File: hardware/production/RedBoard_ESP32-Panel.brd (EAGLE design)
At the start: 242.1 x 248.9 mm, 2454 parts, among them J1 5.5x2.1mm Barrel, J101 USB C, J102 USB_SOLDER_PADS, J103 M10NO_SILK, J108 QWIIC_RIGHT_ANGLE, J109 MICRO-SDPUSH-PUSH, J110 5.5x2.1mm Barrel, J117 USB C, J118 USB_SOLDER_PADS, J119 M10NO_SILK, J124 QWIIC_RIGHT_ANGLE, J125 MICRO-SDPUSH-PUSH, J126 5.5x2.1mm Barrel, J13 QWIIC_RIGHT_ANGLE, J133 USB C, J134 USB_SOLDER_PADS, J135 M10NO_SILK, J140 QWIIC_RIGHT_ANGLE, J141 MICRO-SDPUSH-PUSH, J142 5.5x2.1mm Barrel, J149 USB C, J15 MICRO-SDPUSH-PUSH, J150 USB_SOLDER_PADS, J151 M10NO_SILK, J156 QWIIC_RIGHT_ANGLE, J157 MICRO-SDPUSH-PUSH, J158 5.5x2.1mm Barrel, J165 USB C, J166 USB_SOLDER_PADS, J167 M10NO_SILK, J172 QWIIC_RIGHT_ANGLE, J173 MICRO-SDPUSH-PUSH, J174 5.5x2.1mm Barrel, J181 USB C, J182 USB_SOLDER_PADS, J183 M10NO_SILK, J188 QWIIC_RIGHT_ANGLE, J189 MICRO-SDPUSH-PUSH, J190 5.5x2.1mm Barrel, J2 USB C, J21 USB C, J22 USB_SOLDER_PADS, J23 M10NO_SILK, J28 QWIIC_RIGHT_ANGLE, J29 MICRO-SDPUSH-PUSH, J3 USB_SOLDER_PADS, J30 5.5x2.1mm Barrel, J37 USB C, J38 USB_SOLDER_PADS, J39 M10NO_SILK, J44 QWIIC_RIGHT_ANGLE, J45 MICRO-SDPUSH-PUSH, J46 5.5x2.1mm Barrel, J5 M10NO_SILK, J53 USB C, J54 USB_SOLDER_PADS, J55 M10NO_SILK, J60 QWIIC_RIGHT_ANGLE, J61 MICRO-SDPUSH-PUSH, J62 5.5x2.1mm Barrel, J69 USB C, J70 USB_SOLDER_PADS, J71 M10NO_SILK, J76 QWIIC_RIGHT_ANGLE, J77 MICRO-SDPUSH-PUSH, J78 5.5x2.1mm Barrel, J85 USB C, J86 USB_SOLDER_PADS, J87 M10NO_SILK, J92 QWIIC_RIGHT_ANGLE, J93 MICRO-SDPUSH-PUSH, J94 5.5x2.1mm Barrel, Q1 MBT3904DW1T1, Q100 20V/4.2A/52mΩ/1.4W, Q102 20V/4.2A/52mΩ/1.4W, Q104 20V/4.2A/52mΩ/1.4W, Q105 MBT3904DW1T1, Q107 20V/4.2A/52mΩ/1.4W, Q109 20V/4.2A/52mΩ/1.4W, Q11 20V/4.2A/52mΩ/1.4W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

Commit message: Changed board per Nathan's recommendations; added production files.
- Changed SPI pins nomenclatures.
- Fixed silkscreens.
- Replaced SD card socket with an updated one.
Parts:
- J109, J125, J141, J15, J157, J173, J189, J29, J45, J61, J77, J93: value MICRO-SDPUSH-PUSH -> MICRO-SD-PUSH-PUSH-EXT-PIN; device SparkFun-Connectors:MICRO-SD-SOCKET -> SparkFun-Connectors:MICROSD-EXTERNALPIN
- J111, J112, J127, J128, J14, J143, J144, J159, J16, J160, J175, J176, J191, J192, J31, J32, J47, J48, J63, J64, J79, J80, J95, J96: device SparkFun-Connectors:1X02 -> SparkFun-Connectors:1X02_NO_SILK
- U$1000, U$1094, U$154, U$248, U$342, U$436, U$530, U$62, U$624, U$718, U$812, U$906: device output-ESP32:#IOREF#32321868 -> output-ESP32:#IOREF#321865
- U$101, U$1041, U$195, U$289, U$383, U$477, U$571, U$665, U$759, U$8, U$853, U$947: device output-ESP32:#CIPO#30 -> output-ESP32:#POCI#30
- U$1010, U$1104, U$164, U$258, U$352, U$446, U$540, U$634, U$728, U$73, U$822, U$916: device output-ESP32:#23#COPI#32321869 -> output-ESP32:#23#PICO#321866
- U$1011, U$1105, U$165, U$259, U$353, U$447, U$541, U$635, U$729, U$74, U$823, U$917: device output-ESP32:#19#CIPO#32321869 -> output-ESP32:#19#POCI#321866
- U$1016, U$1110, U$170, U$264, U$358, U$452, U$546, U$640, U$734, U$79, U$828, U$922: device output-ESP32:#GND#32321869 -> output-ESP32:#GND#321866
- U$1017, U$1111, U$171, U$265, U$359, U$453, U$547, U$641, U$735, U$80, U$829, U$923: device output-ESP32:#3#3V#32321869 -> output-ESP32:#3#3V#321866
- U$102, U$1042, U$196, U$290, U$384, U$478, U$572, U$666, U$760, U$854, U$9, U$948: device output-ESP32:#COPI#29 -> output-ESP32:#PICO#29
- U$1082, U$142, U$236, U$330, U$424, U$50, U$518, U$612, U$706, U$800, U$894, U$988: device output-ESP32:#39#A3#32321865 -> output-ESP32:#39#A3#321862
- U$1083, U$143, U$237, U$331, U$425, U$51, U$519, U$613, U$707, U$801, U$895, U$989: device output-ESP32:#36#A0#32321865 -> output-ESP32:#36#A0#321862
- U$1085, U$145, U$239, U$333, U$427, U$521, U$53, U$615, U$709, U$803, U$897, U$991: device output-ESP32:#35#A7#32321865 -> output-ESP32:#35#A7#321862
- U$1087, U$147, U$241, U$335, U$429, U$523, U$55, U$617, U$711, U$805, U$899, U$993: device output-ESP32:#33#A5#32321865 -> output-ESP32:#34#A6#321862
- U$1088, U$148, U$242, U$336, U$430, U$524, U$56, U$618, U$712, U$806, U$900, U$994: device output-ESP32:#VIN#32321865 -> output-ESP32:#VIN#321862
- U$1089, U$1092, U$149, U$152, U$243, U$246, U$337, U$340, U$431, U$434, U$525, U$528, U$57, U$60, U$619, U$622, U$713, U$716, U$807, U$810, U$901, U$904, U$995, U$998: device output-ESP32:#GND#32321866 -> output-ESP32:#GND#321863
- U$1090, U$150, U$244, U$338, U$432, U$526, U$58, U$620, U$714, U$808, U$902, U$996: device output-ESP32:#5V#32321867 -> output-ESP32:#5V#321864
- U$1091, U$151, U$245, U$339, U$433, U$527, U$59, U$621, U$715, U$809, U$903, U$997: device output-ESP32:#3#3V#32321867 -> output-ESP32:#3#3V#321864
- U$1093, U$153, U$247, U$341, U$435, U$529, U$61, U$623, U$717, U$811, U$905, U$999: device output-ESP32:##RST##32321867 -> output-ESP32:##RESET##321864
- moved R173 39.3 mm to (200.2, 64.0), turned to 270 degrees
- moved R260 39.3 mm to (200.2, 122.9), turned to 270 degrees
- moved R347 39.3 mm to (200.2, 181.9), turned to 270 degrees
- moved R86 39.3 mm to (200.2, 5.08), turned to 270 degrees
- moved LOGO1 36.8 mm to (15.4, 28.4), turned to 270 degrees
- moved LOGO16 36.8 mm to (15.4, 87.4), turned to 270 degrees
- moved LOGO31 36.8 mm to (15.4, 146.3), turned to 270 degrees
- moved LOGO46 36.8 mm to (15.4, 205.2), turned to 270 degrees
- moved R144 36.3 mm to (124.2, 64.0), turned to 270 degrees
- moved R231 36.3 mm to (124.2, 122.9), turned to 270 degrees
- moved R318 36.3 mm to (124.2, 181.9), turned to 270 degrees
- moved R57 36.3 mm to (124.2, 5.08), turned to 270 degrees
- moved LOGO21 34.1 mm to (91.3, 87.4), turned to 270 degrees
- moved LOGO5 34.1 mm to (91.3, 28.4), turned to 270 degrees
- moved LOGO36 34.1 mm to (91.3, 146.3), turned to 270 degrees
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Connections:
- removed net ESP32_GPIO19_CIPO: J15.DO/DAT0, J5.6, J6.6A, J6.6B, U1.31
- removed net ESP32_GPIO19_CIPO1: J17.6A, J17.6B, J23.6, J29.DO/DAT0, U8.31
- removed net ESP32_GPIO19_CIPO10: J161.6A, J161.6B, J167.6, J173.DO/DAT0, U62.31
- removed net ESP32_GPIO19_CIPO11: J177.6A, J177.6B, J183.6, J189.DO/DAT0, U68.31
- removed net ESP32_GPIO19_CIPO2: J33.6A, J33.6B, J39.6, J45.DO/DAT0, U14.31
- removed net ESP32_GPIO19_CIPO3: J49.6A, J49.6B, J55.6, J61.DO/DAT0, U20.31
- removed net ESP32_GPIO19_CIPO4: J65.6A, J65.6B, J71.6, J77.DO/DAT0, U26.31
- removed net ESP32_GPIO19_CIPO5: J81.6A, J81.6B, J87.6, J93.DO/DAT0, U32.31
- removed net ESP32_GPIO19_CIPO6: J103.6, J109.DO/DAT0, J97.6A, J97.6B, U38.31
- removed net ESP32_GPIO19_CIPO7: J113.6A, J113.6B, J119.6, J125.DO/DAT0, U44.31
- removed net ESP32_GPIO19_CIPO8: J129.6A, J129.6B, J135.6, J141.DO/DAT0, U50.31
- removed net ESP32_GPIO19_CIPO9: J145.6A, J145.6B, J151.6, J157.DO/DAT0, U56.31
- removed net ESP32_GPIO23_COPI: J15.DI/CMD, J5.7, J6.7A, J6.7B, U1.37
- removed net ESP32_GPIO23_COPI1: J17.7A, J17.7B, J23.7, J29.DI/CMD, U8.37
- removed net ESP32_GPIO23_COPI10: J161.7A, J161.7B, J167.7, J173.DI/CMD, U62.37
- removed net ESP32_GPIO23_COPI11: J177.7A, J177.7B, J183.7, J189.DI/CMD, U68.37
- removed net ESP32_GPIO23_COPI2: J33.7A, J33.7B, J39.7, J45.DI/CMD, U14.37
- removed net ESP32_GPIO23_COPI3: J49.7A, J49.7B, J55.7, J61.DI/CMD, U20.37
- removed net ESP32_GPIO23_COPI4: J65.7A, J65.7B, J71.7, J77.DI/CMD, U26.37
- removed net ESP32_GPIO23_COPI5: J81.7A, J81.7B, J87.7, J93.DI/CMD, U32.37
- removed net ESP32_GPIO23_COPI6: J103.7, J109.DI/CMD, J97.7A, J97.7B, U38.37
- removed net ESP32_GPIO23_COPI7: J113.7A, J113.7B, J119.7, J125.DI/CMD, U44.37
- removed net ESP32_GPIO23_COPI8: J129.7A, J129.7B, J135.7, J141.DI/CMD, U50.37
- removed net ESP32_GPIO23_COPI9: J145.7A, J145.7B, J151.7, J157.DI/CMD, U56.37
- removed net GND1: C18.2, C19.2, C20.-, C21.2, C22.2, C23.2, C24.2, C25.2, C26.-, C27.2, C28.-, C29.2, C30.2, C31.2, C32.2, C33.2, C34.2, J17.4A, J17.4B, J18.6, J18.7, J21.GND, J21.GND2, J22.GND, J23.4, J24.6, J24.7, J27.3, J27.5, J27.7, J27.9, J28.1, J29.GND, J29.GND1, J29.GND3, J30.GND, J32.2, JP27.1, Q17.1, Q17.4, R32.1, R33.1, R37.1, R40.1, R42.1, R43.1, R47.1, R48.1, R49.1, R50.1, R52.1, R53.1, R54.1, R55.1, R56.1, R58.1, S3.1, S3.2, S4.1, S4.2, U10.2, U11.2, U12.1, U12.4, U12.6, U12.9, U7.1, U8.1, U8.15, U8.38, U8.GND1, U8.GNDT1, U8.GNDT2, U8.GNDT3, U8.GNDT4, U8.GNDT5, U8.GNDT6, U8.GNDT7, U8.GNDT8
- removed net GND11: C188.2, C189.2, C190.-, C191.2, C192.2, C193.2, C194.2, C195.2, C196.-, C197.2, C198.-, C199.2, C200.2, C201.2, C202.2, C203.2, C204.2, J177.4A, J177.4B, J178.6, J178.7, J181.GND, J181.GND2, J182.GND, J183.4, J184.6, J184.7, J187.3, J187.5, J187.7, J187.9, J188.1, J189.GND, J189.GND1, J189.GND3, J190.GND, J192.2, JP167.1, Q147.1, Q147.4, R322.1, R323.1, R327.1, R330.1, R332.1, R333.1, R337.1, R338.1, R339.1, R340.1, R342.1, R343.1, R344.1, R345.1, R346.1, R348.1, S23.1, S23.2, S24.1, S24.2, U67.1, U68.1, U68.15, U68.38, U68.GND1, U68.GNDT1, U68.GNDT2, U68.GNDT3, U68.GNDT4, U68.GNDT5, U68.GNDT6, U68.GNDT7, U68.GNDT8, U70.2, U71.2, U72.1, U72.4, U72.6, U72.9
- removed net GND3: C52.2, C53.2, C54.-, C55.2, C56.2, C57.2, C58.2, C59.2, C60.-, C61.2, C62.-, C63.2, C64.2, C65.2, C66.2, C67.2, C68.2, J49.4A, J49.4B, J50.6, J50.7, J53.GND, J53.GND2, J54.GND, J55.4, J56.6, J56.7, J59.3, J59.5, J59.7, J59.9, J60.1, J61.GND, J61.GND1, J61.GND3, J62.GND, J64.2, JP55.1, Q43.1, Q43.4, R100.1, R101.1, R105.1, R106.1, R107.1, R108.1, R110.1, R111.1, R112.1, R113.1, R114.1, R116.1, R90.1, R91.1, R95.1, R98.1, S7.1, S7.2, S8.1, S8.2, U19.1, U20.1, U20.15, U20.38, U20.GND1, U20.GNDT1, U20.GNDT2, U20.GNDT3, U20.GNDT4, U20.GNDT5, U20.GNDT6, U20.GNDT7, U20.GNDT8, U22.2, U23.2, U24.1, U24.4, U24.6, U24.9
- removed net GND5: C100.2, C101.2, C102.2, C86.2, C87.2, C88.-, C89.2, C90.2, C91.2, C92.2, C93.2, C94.-, C95.2, C96.-, C97.2, C98.2, C99.2, J81.4A, J81.4B, J82.6, J82.7, J85.GND, J85.GND2, J86.GND, J87.4, J88.6, J88.7, J91.3, J91.5, J91.7, J91.9, J92.1, J93.GND, J93.GND1, J93.GND3, J94.GND, J96.2, JP83.1, Q69.1, Q69.4, R148.1, R149.1, R153.1, R156.1, R158.1, R159.1, R163.1, R164.1, R165.1, R166.1, R168.1, R169.1, R170.1, R171.1, R172.1, R174.1, S11.1, S11.2, S12.1, S12.2, U31.1, U32.1, U32.15, U32.38, U32.GND1, U32.GNDT1, U32.GNDT2, U32.GNDT3, U32.GNDT4, U32.GNDT5, U32.GNDT6, U32.GNDT7, U32.GNDT8, U34.2, U35.2, U36.1, U36.4, U36.6, U36.9
- removed net GND7: C120.2, C121.2, C122.-, C123.2, C124.2, C125.2, C126.2, C127.2, C128.-, C129.2, C130.-, C131.2, C132.2, C133.2, C134.2, C135.2, C136.2, J113.4A, J113.4B, J114.6, J114.7, J117.GND, J117.GND2, J118.GND, J119.4, J120.6, J120.7, J123.3, J123.5, J123.7, J123.9, J124.1, J125.GND, J125.GND1, J125.GND3, J126.GND, J128.2, JP111.1, Q95.1, Q95.4, R206.1, R207.1, R211.1, R214.1, R216.1, R217.1, R221.1, R222.1, R223.1, R224.1, R226.1, R227.1, R228.1, R229.1, R230.1, R232.1, S15.1, S15.2, S16.1, S16.2, U43.1, U44.1, U44.15, U44.38, U44.GND1, U44.GNDT1, U44.GNDT2, U44.GNDT3, U44.GNDT4, U44.GNDT5, U44.GNDT6, U44.GNDT7, U44.GNDT8, U46.2, U47.2, U48.1, U48.4, U48.6, U48.9
- removed net GND9: C154.2, C155.2, C156.-, C157.2, C158.2, C159.2, C160.2, C161.2, C162.-, C163.2, C164.-, C165.2, C166.2, C167.2, C168.2, C169.2, C170.2, J145.4A, J145.4B, J146.6, J146.7, J149.GND, J149.GND2, J150.GND, J151.4, J152.6, J152.7, J155.3, J155.5, J155.7, J155.9, J156.1, J157.GND, J157.GND1, J157.GND3, J158.GND, J160.2, JP139.1, Q121.1, Q121.4, R264.1, R265.1, R269.1, R272.1, R274.1, R275.1, R279.1, R280.1, R281.1, R282.1, R284.1, R285.1, R286.1, R287.1, R288.1, R290.1, S19.1, S19.2, S20.1, S20.2, U55.1, U56.1, U56.15, U56.38, U56.GND1, U56.GNDT1, U56.GNDT2, U56.GNDT3, U56.GNDT4, U56.GNDT5, U56.GNDT6, U56.GNDT7, U56.GNDT8, U58.2, U59.2, U60.1, U60.4, U60.6, U60.9
- new net ESP32_GPIO19_POCI: J15.7, J5.6, J6.6A, J6.6B, U1.31
- new net ESP32_GPIO19_POCI1: J17.6A, J17.6B, J23.6, J29.7, U8.31
- new net ESP32_GPIO19_POCI10: J161.6A, J161.6B, J167.6, J173.7, U62.31
- new net ESP32_GPIO19_POCI11: J177.6A, J177.6B, J183.6, J189.7, U68.31
- new net ESP32_GPIO19_POCI2: J33.6A, J33.6B, J39.6, J45.7, U14.31
- new net ESP32_GPIO19_POCI3: J49.6A, J49.6B, J55.6, J61.7, U20.31
- new net ESP32_GPIO19_POCI4: J65.6A, J65.6B, J71.6, J77.7, U26.31
- new net ESP32_GPIO19_POCI5: J81.6A, J81.6B, J87.6, J93.7, U32.31
- new net ESP32_GPIO19_POCI6: J103.6, J109.7, J97.6A, J97.6B, U38.31
- new net ESP32_GPIO19_POCI7: J113.6A, J113.6B, J119.6, J125.7, U44.31
- new net ESP32_GPIO19_POCI8: J129.6A, J129.6B, J135.6, J141.7, U50.31
- new net ESP32_GPIO19_POCI9: J145.6A, J145.6B, J151.6, J157.7, U56.31
- new net ESP32_GPIO23_PICO: J15.3, J5.7, J6.7A, J6.7B, U1.37
- new net ESP32_GPIO23_PICO1: J17.7A, J17.7B, J23.7, J29.3, U8.37
- new net ESP32_GPIO23_PICO10: J161.7A, J161.7B, J167.7, J173.3, U62.37
- new net ESP32_GPIO23_PICO11: J177.7A, J177.7B, J183.7, J189.3, U68.37
- new net ESP32_GPIO23_PICO2: J33.7A, J33.7B, J39.7, J45.3, U14.37
- new net ESP32_GPIO23_PICO3: J49.7A, J49.7B, J55.7, J61.3, U20.37
- new net ESP32_GPIO23_PICO4: J65.7A, J65.7B, J71.7, J77.3, U26.37
- new net ESP32_GPIO23_PICO5: J81.7A, J81.7B, J87.7, J93.3, U32.37
- new net ESP32_GPIO23_PICO6: J103.7, J109.3, J97.7A, J97.7B, U38.37
- new net ESP32_GPIO23_PICO7: J113.7A, J113.7B, J119.7, J125.3, U44.37
- new net ESP32_GPIO23_PICO8: J129.7A, J129.7B, J135.7, J141.3, U50.37
- new net ESP32_GPIO23_PICO9: J145.7A, J145.7B, J151.7, J157.3, U56.37
- new net GND12: C103.2, C104.2, C105.-, C106.2, C107.2, C108.2, C109.2, C110.2, C111.-, C112.2, C113.-, C114.2, C115.2, C116.2, C117.2, C118.2, C119.2, J101.GND, J101.GND2, J102.GND, J103.4, J104.6, J104.7, J107.3, J107.5, J107.7, J107.9, J108.1, J109.10, J109.11, J109.12, J109.13, J109.6, J110.GND, J112.2, J97.4A, J97.4B, J98.6, J98.7, JP97.1, Q82.1, Q82.4, R177.1, R178.1, R182.1, R185.1, R187.1, R188.1, R192.1, R193.1, R194.1, R195.1, R197.1, R198.1, R199.1, R200.1, R201.1, R203.1, S13.1, S13.2, S14.1, S14.2, U37.1, U38.1, U38.15, U38.38, U38.GND1, U38.GNDT1, U38.GNDT2, U38.GNDT3, U38.GNDT4, U38.GNDT5, U38.GNDT6, U38.GNDT7, U38.GNDT8, U40.2, U41.2, U42.1, U42.4, U42.6, U42.9
- new net GND14: C120.2, C121.2, C122.-, C123.2, C124.2, C125.2, C126.2, C127.2, C128.-, C129.2, C130.-, C131.2, C132.2, C133.2, C134.2, C135.2, C136.2, J113.4A, J113.4B, J114.6, J114.7, J117.GND, J117.GND2, J118.GND, J119.4, J120.6, J120.7, J123.3, J123.5, J123.7, J123.9, J124.1, J125.10, J125.11, J125.12, J125.13, J125.6, J126.GND, J128.2, JP111.1, Q95.1, Q95.4, R206.1, R207.1, R211.1, R214.1, R216.1, R217.1, R221.1, R222.1, R223.1, R224.1, R226.1, R227.1, R228.1, R229.1, R230.1, R232.1, S15.1, S15.2, S16.1, S16.2, U43.1, U44.1, U44.15, U44.38, U44.GND1, U44.GNDT1, U44.GNDT2, U44.GNDT3, U44.GNDT4, U44.GNDT5, U44.GNDT6, U44.GNDT7, U44.GNDT8, U46.2, U47.2, U48.1, U48.4, U48.6, U48.9
- new net GND16: C137.2, C138.2, C139.-, C140.2, C141.2, C142.2, C143.2, C144.2, C145.-, C146.2, C147.-, C148.2, C149.2, C150.2, C151.2, C152.2, C153.2, J129.4A, J129.4B, J130.6, J130.7, J133.GND, J133.GND2, J134.GND, J135.4, J136.6, J136.7, J139.3, J139.5, J139.7, J139.9, J140.1, J141.10, J141.11, J141.12, J141.13, J141.6, J142.GND, J144.2, JP125.1, Q108.1, Q108.4, R235.1, R236.1, R240.1, R243.1, R245.1, R246.1, R250.1, R251.1, R252.1, R253.1, R255.1, R256.1, R257.1, R258.1, R259.1, R261.1, S17.1, S17.2, S18.1, S18.2, U49.1, U50.1, U50.15, U50.38, U50.GND1, U50.GNDT1, U50.GNDT2, U50.GNDT3, U50.GNDT4, U50.GNDT5, U50.GNDT6, U50.GNDT7, U50.GNDT8, U52.2, U53.2, U54.1, U54.4, U54.6, U54.9
- new net GND18: C154.2, C155.2, C156.-, C157.2, C158.2, C159.2, C160.2, C161.2, C162.-, C163.2, C164.-, C165.2, C166.2, C167.2, C168.2, C169.2, C170.2, J145.4A, J145.4B, J146.6, J146.7, J149.GND, J149.GND2, J150.GND, J151.4, J152.6, J152.7, J155.3, J155.5, J155.7, J155.9, J156.1, J157.10, J157.11, J157.12, J157.13, J157.6, J158.GND, J160.2, JP139.1, Q121.1, Q121.4, R264.1, R265.1, R269.1, R272.1, R274.1, R275.1, R279.1, R280.1, R281.1, R282.1, R284.1, R285.1, R286.1, R287.1, R288.1, R290.1, S19.1, S19.2, S20.1, S20.2, U55.1, U56.1, U56.15, U56.38, U56.GND1, U56.GNDT1, U56.GNDT2, U56.GNDT3, U56.GNDT4, U56.GNDT5, U56.GNDT6, U56.GNDT7, U56.GNDT8, U58.2, U59.2, U60.1, U60.4, U60.6, U60.9
- new net GND20: C171.2, C172.2, C173.-, C174.2, C175.2, C176.2, C177.2, C178.2, C179.-, C180.2, C181.-, C182.2, C183.2, C184.2, C185.2, C186.2, C187.2, J161.4A, J161.4B, J162.6, J162.7, J165.GND, J165.GND2, J166.GND, J167.4, J168.6, J168.7, J171.3, J171.5, J171.7, J171.9, J172.1, J173.10, J173.11, J173.12, J173.13, J173.6, J174.GND, J176.2, JP153.1, Q134.1, Q134.4, R293.1, R294.1, R298.1, R301.1, R303.1, R304.1, R308.1, R309.1, R310.1, R311.1, R313.1, R314.1, R315.1, R316.1, R317.1, R319.1, S21.1, S21.2, S22.1, S22.2, U61.1, U62.1, U62.15, U62.38, U62.GND1, U62.GNDT1, U62.GNDT2, U62.GNDT3, U62.GNDT4, U62.GNDT5, U62.GNDT6, U62.GNDT7, U62.GNDT8, U64.2, U65.2, U66.1, U66.4, U66.6, U66.9
- new net GND22: C188.2, C189.2, C190.-, C191.2, C192.2, C193.2, C194.2, C195.2, C196.-, C197.2, C198.-, C199.2, C200.2, C201.2, C202.2, C203.2, C204.2, J177.4A, J177.4B, J178.6, J178.7, J181.GND, J181.GND2, J182.GND, J183.4, J184.6, J184.7, J187.3, J187.5, J187.7, J187.9, J188.1, J189.10, J189.11, J189.12, J189.13, J189.6, J190.GND, J192.2, JP167.1, Q147.1, Q147.4, R322.1, R323.1, R327.1, R330.1, R332.1, R333.1, R337.1, R338.1, R339.1, R340.1, R342.1, R343.1, R344.1, R345.1, R346.1, R348.1, S23.1, S23.2, S24.1, S24.2, U67.1, U68.1, U68.15, U68.38, U68.GND1, U68.GNDT1, U68.GNDT2, U68.GNDT3, U68.GNDT4, U68.GNDT5, U68.GNDT6, U68.GNDT7, U68.GNDT8, U70.2, U71.2, U72.1, U72.4, U72.6, U72.9
- net 3.3V: now also J15.4; no longer J15.VCC
- net 3.3V1: now also J29.4; no longer J29.VCC
- net 3.3V10: now also J173.4; no longer J173.VCC
- net 3.3V11: now also J189.4; no longer J189.VCC
- net 3.3V2: now also J45.4; no longer J45.VCC
- net 3.3V3: now also J61.4; no longer J61.VCC
- net 3.3V4: now also J77.4; no longer J77.VCC
- net 3.3V5: now also J93.4; no longer J93.VCC
- net 3.3V6: now also J109.4; no longer J109.VCC
- net 3.3V7: now also J125.4; no longer J125.VCC
- net 3.3V8: now also J141.4; no longer J141.VCC
- net 3.3V9: now also J157.4; no longer J157.VCC
- net ESP32_GPIO18_SCK: now also J15.5; no longer J15.SCLK
- net ESP32_GPIO18_SCK1: now also J29.5; no longer J29.SCLK
- net ESP32_GPIO18_SCK10: now also J173.5; no longer J173.SCLK
- net ESP32_GPIO18_SCK11: now also J189.5; no longer J189.SCLK
- net ESP32_GPIO18_SCK2: now also J45.5; no longer J45.SCLK
- net ESP32_GPIO18_SCK3: now also J61.5; no longer J61.SCLK
- net ESP32_GPIO18_SCK4: now also J77.5; no longer J77.SCLK
- net ESP32_GPIO18_SCK5: now also J93.5; no longer J93.SCLK
- net ESP32_GPIO18_SCK6: now also J109.5; no longer J109.SCLK
- net ESP32_GPIO18_SCK7: now also J125.5; no longer J125.SCLK
- net ESP32_GPIO18_SCK8: now also J141.5; no longer J141.SCLK
- net ESP32_GPIO18_SCK9: now also J157.5; no longer J157.SCLK
- net ESP32_GPIO5_!CS!: now also J15.2; no longer J15.CS/DAT3
- net ESP32_GPIO5_!CS!1: now also J29.2; no longer J29.CS/DAT3
- net ESP32_GPIO5_!CS!10: now also J173.2; no longer J173.CS/DAT3
- net ESP32_GPIO5_!CS!11: now also J189.2; no longer J189.CS/DAT3
- net ESP32_GPIO5_!CS!2: now also J45.2; no longer J45.CS/DAT3
- net ESP32_GPIO5_!CS!3: now also J61.2; no longer J61.CS/DAT3
- net ESP32_GPIO5_!CS!4: now also J77.2; no longer J77.CS/DAT3
- net ESP32_GPIO5_!CS!5: now also J93.2; no longer J93.CS/DAT3
- net ESP32_GPIO5_!CS!6: now also J109.2; no longer J109.CS/DAT3
- net ESP32_GPIO5_!CS!7: now also J125.2; no longer J125.CS/DAT3
- net ESP32_GPIO5_!CS!8: now also J141.2; no longer J141.CS/DAT3
- net ESP32_GPIO5_!CS!9: now also J157.2; no longer J157.CS/DAT3
- net GND: now also J15.10, J15.11, J15.12, J15.13, J15.6; no longer J15.GND, J15.GND1, J15.GND3
- net GND10: now also C100.2, C101.2, C102.2, C86.2, C87.2, C88.-, C89.2, C90.2, C91.2, C92.2, C93.2, C94.-, C95.2, C96.-, C97.2, C98.2, C99.2, J81.4A, J81.4B, J82.6, J82.7, J85.GND, J85.GND2, J86.GND, J87.4, J88.6, J88.7, J91.3, J91.5, J91.7, J91.9, J92.1, J93.10, J93.11, J93.12, J93.13, J93.6, J94.GND, J96.2, JP83.1, Q69.1, Q69.4, R148.1, R149.1, R153.1, R156.1, R158.1, R159.1, R163.1, R164.1, R165.1, R166.1, R168.1, R169.1, R170.1, R171.1, R172.1, R174.1, S11.1, S11.2, S12.1, S12.2, U31.1, U32.1, U32.15, U32.38, U32.GND1, U32.GNDT1, U32.GNDT2, U32.GNDT3, U32.GNDT4, U32.GNDT5, U32.GNDT6, U32.GNDT7, U32.GNDT8, U34.2, U35.2, U36.1, U36.4, U36.6, U36.9; no longer C171.2, C172.2, C173.-, C174.2, C175.2, C176.2, C177.2, C178.2, C179.-, C180.2, C181.-, C182.2, C183.2, C184.2, C185.2, C186.2, C187.2, J161.4A, J161.4B, J162.6, J162.7, J165.GND, J165.GND2, J166.GND, J167.4, J168.6, J168.7, J171.3, J171.5, J171.7, J171.9, J172.1, J173.GND, J173.GND1, J173.GND3, J174.GND, J176.2, JP153.1, Q134.1, Q134.4, R293.1, R294.1, R298.1, R301.1, R303.1, R304.1, R308.1, R309.1, R310.1, R311.1, R313.1, R314.1, R315.1, R316.1, R317.1, R319.1, S21.1, S21.2, S22.1, S22.2, U61.1, U62.1, U62.15, U62.38, U62.GND1, U62.GNDT1, U62.GNDT2, U62.GNDT3, U62.GNDT4, U62.GNDT5, U62.GNDT6, U62.GNDT7, U62.GNDT8, U64.2, U65.2, U66.1, U66.4, U66.6, U66.9
- net GND2: now also C18.2, C19.2, C20.-, C21.2, C22.2, C23.2, C24.2, C25.2, C26.-, C27.2, C28.-, C29.2, C30.2, C31.2, C32.2, C33.2, C34.2, J17.4A, J17.4B, J18.6, J18.7, J21.GND, J21.GND2, J22.GND, J23.4, J24.6, J24.7, J27.3, J27.5, J27.7, J27.9, J28.1, J29.10, J29.11, J29.12, J29.13, J29.6, J30.GND, J32.2, JP27.1, Q17.1, Q17.4, R32.1, R33.1, R37.1, R40.1, R42.1, R43.1, R47.1, R48.1, R49.1, R50.1, R52.1, R53.1, R54.1, R55.1, R56.1, R58.1, S3.1, S3.2, S4.1, S4.2, U10.2, U11.2, U12.1, U12.4, U12.6, U12.9, U7.1, U8.1, U8.15, U8.38, U8.GND1, U8.GNDT1, U8.GNDT2, U8.GNDT3, U8.GNDT4, U8.GNDT5, U8.GNDT6, U8.GNDT7, U8.GNDT8; no longer C35.2, C36.2, C37.-, C38.2, C39.2, C40.2, C41.2, C42.2, C43.-, C44.2, C45.-, C46.2, C47.2, C48.2, C49.2, C50.2, C51.2, J33.4A, J33.4B, J34.6, J34.7, J37.GND, J37.GND2, J38.GND, J39.4, J40.6, J40.7, J43.3, J43.5, J43.7, J43.9, J44.1, J45.GND, J45.GND1, J45.GND3, J46.GND, J48.2, JP41.1, Q30.1, Q30.4, R61.1, R62.1, R66.1, R69.1, R71.1, R72.1, R76.1, R77.1, R78.1, R79.1, R81.1, R82.1, R83.1, R84.1, R85.1, R87.1, S5.1, S5.2, S6.1, S6.2, U13.1, U14.1, U14.15, U14.38, U14.GND1, U14.GNDT1, U14.GNDT2, U14.GNDT3, U14.GNDT4, U14.GNDT5, U14.GNDT6, U14.GNDT7, U14.GNDT8, U16.2, U17.2, U18.1, U18.4, U18.6, U18.9
- net GND4: now also C35.2, C36.2, C37.-, C38.2, C39.2, C40.2, C41.2, C42.2, C43.-, C44.2, C45.-, C46.2, C47.2, C48.2, C49.2, C50.2, C51.2, J33.4A, J33.4B, J34.6, J34.7, J37.GND, J37.GND2, J38.GND, J39.4, J40.6, J40.7, J43.3, J43.5, J43.7, J43.9, J44.1, J45.10, J45.11, J45.12, J45.13, J45.6, J46.GND, J48.2, JP41.1, Q30.1, Q30.4, R61.1, R62.1, R66.1, R69.1, R71.1, R72.1, R76.1, R77.1, R78.1, R79.1, R81.1, R82.1, R83.1, R84.1, R85.1, R87.1, S5.1, S5.2, S6.1, S6.2, U13.1, U14.1, U14.15, U14.38, U14.GND1, U14.GNDT1, U14.GNDT2, U14.GNDT3, U14.GNDT4, U14.GNDT5, U14.GNDT6, U14.GNDT7, U14.GNDT8, U16.2, U17.2, U18.1, U18.4, U18.6, U18.9; no longer C69.2, C70.2, C71.-, C72.2, C73.2, C74.2, C75.2, C76.2, C77.-, C78.2, C79.-, C80.2, C81.2, C82.2, C83.2, C84.2, C85.2, J65.4A, J65.4B, J66.6, J66.7, J69.GND, J69.GND2, J70.GND, J71.4, J72.6, J72.7, J75.3, J75.5, J75.7, J75.9, J76.1, J77.GND, J77.GND1, J77.GND3, J78.GND, J80.2, JP69.1, Q56.1, Q56.4, R119.1, R120.1, R124.1, R127.1, R129.1, R130.1, R134.1, R135.1, R136.1, R137.1, R139.1, R140.1, R141.1, R142.1, R143.1, R145.1, S10.1, S10.2, S9.1, S9.2, U25.1, U26.1, U26.15, U26.38, U26.GND1, U26.GNDT1, U26.GNDT2, U26.GNDT3, U26.GNDT4, U26.GNDT5, U26.GNDT6, U26.GNDT7, U26.GNDT8, U28.2, U29.2, U30.1, U30.4, U30.6, U30.9
- net GND6: now also C52.2, C53.2, C54.-, C55.2, C56.2, C57.2, C58.2, C59.2, C60.-, C61.2, C62.-, C63.2, C64.2, C65.2, C66.2, C67.2, C68.2, J49.4A, J49.4B, J50.6, J50.7, J53.GND, J53.GND2, J54.GND, J55.4, J56.6, J56.7, J59.3, J59.5, J59.7, J59.9, J60.1, J61.10, J61.11, J61.12, J61.13, J61.6, J62.GND, J64.2, JP55.1, Q43.1, Q43.4, R100.1, R101.1, R105.1, R106.1, R107.1, R108.1, R110.1, R111.1, R112.1, R113.1, R114.1, R116.1, R90.1, R91.1, R95.1, R98.1, S7.1, S7.2, S8.1, S8.2, U19.1, U20.1, U20.15, U20.38, U20.GND1, U20.GNDT1, U20.GNDT2, U20.GNDT3, U20.GNDT4, U20.GNDT5, U20.GNDT6, U20.GNDT7, U20.GNDT8, U22.2, U23.2, U24.1, U24.4, U24.6, U24.9; no longer C103.2, C104.2, C105.-, C106.2, C107.2, C108.2, C109.2, C110.2, C111.-, C112.2, C113.-, C114.2, C115.2, C116.2, C117.2, C118.2, C119.2, J101.GND, J101.GND2, J102.GND, J103.4, J104.6, J104.7, J107.3, J107.5, J107.7, J107.9, J108.1, J109.GND, J109.GND1, J109.GND3, J110.GND, J112.2, J97.4A, J97.4B, J98.6, J98.7, JP97.1, Q82.1, Q82.4, R177.1, R178.1, R182.1, R185.1, R187.1, R188.1, R192.1, R193.1, R194.1, R195.1, R197.1, R198.1, R199.1, R200.1, R201.1, R203.1, S13.1, S13.2, S14.1, S14.2, U37.1, U38.1, U38.15, U38.38, U38.GND1, U38.GNDT1, U38.GNDT2, U38.GNDT3, U38.GNDT4, U38.GNDT5, U38.GNDT6, U38.GNDT7, U38.GNDT8, U40.2, U41.2, U42.1, U42.4, U42.6, U42.9
- net GND8: now also C69.2, C70.2, C71.-, C72.2, C73.2, C74.2, C75.2, C76.2, C77.-, C78.2, C79.-, C80.2, C81.2, C82.2, C83.2, C84.2, C85.2, J65.4A, J65.4B, J66.6, J66.7, J69.GND, J69.GND2, J70.GND, J71.4, J72.6, J72.7, J75.3, J75.5, J75.7, J75.9, J76.1, J77.10, J77.11, J77.12, J77.13, J77.6, J78.GND, J80.2, JP69.1, Q56.1, Q56.4, R119.1, R120.1, R124.1, R127.1, R129.1, R130.1, R134.1, R135.1, R136.1, R137.1, R139.1, R140.1, R141.1, R142.1, R143.1, R145.1, S10.1, S10.2, S9.1, S9.2, U25.1, U26.1, U26.15, U26.38, U26.GND1, U26.GNDT1, U26.GNDT2, U26.GNDT3, U26.GNDT4, U26.GNDT5, U26.GNDT6, U26.GNDT7, U26.GNDT8, U28.2, U29.2, U30.1, U30.4, U30.6, U30.9; no longer C137.2, C138.2, C139.-, C140.2, C141.2, C142.2, C143.2, C144.2, C145.-, C146.2, C147.-, C148.2, C149.2, C150.2, C151.2, C152.2, C153.2, J129.4A, J129.4B, J130.6, J130.7, J133.GND, J133.GND2, J134.GND, J135.4, J136.6, J136.7, J139.3, J139.5, J139.7, J139.9, J140.1, J141.GND, J141.GND1, J141.GND3, J142.GND, J144.2, JP125.1, Q108.1, Q108.4, R235.1, R236.1, R240.1, R243.1, R245.1, R246.1, R250.1, R251.1, R252.1, R253.1, R255.1, R256.1, R257.1, R258.1, R259.1, R261.1, S17.1, S17.2, S18.1, S18.2, U49.1, U50.1, U50.15, U50.38, U50.GND1, U50.GNDT1, U50.GNDT2, U50.GNDT3, U50.GNDT4, U50.GNDT5, U50.GNDT6, U50.GNDT7, U50.GNDT8, U52.2, U53.2, U54.1, U54.4, U54.6, U54.9
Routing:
- net ESP32_GPIO19_POCI8: track 0.00 -> 149.6 mm, vias 0 -> 5
- net ESP32_GPIO19_POCI5: track 0.00 -> 149.6 mm, vias 0 -> 5
- net ESP32_GPIO19_POCI2: track 0.00 -> 149.6 mm, vias 0 -> 5
- net ESP32_GPIO19_POCI11: track 0.00 -> 149.6 mm, vias 0 -> 5
- net ESP32_GPIO19_POCI6: track 0.00 -> 149.6 mm, vias 0 -> 5
- net ESP32_GPIO19_POCI9: track 0.00 -> 149.6 mm, vias 0 -> 5
- net ESP32_GPIO19_POCI7: track 0.00 -> 149.6 mm, vias 0 -> 5
- net ESP32_GPIO19_POCI4: track 0.00 -> 149.6 mm, vias 0 -> 5
- net ESP32_GPIO19_POCI3: track 0.00 -> 149.6 mm, vias 0 -> 5
- net ESP32_GPIO19_POCI10: track 0.00 -> 149.6 mm, vias 0 -> 5
- net ESP32_GPIO19_POCI1: track 0.00 -> 149.6 mm, vias 0 -> 5
- net ESP32_GPIO19_POCI: track 0.00 -> 149.6 mm, vias 0 -> 5
- net ESP32_GPIO19_CIPO1: track 143.9 -> 0.00 mm, vias 5 -> 0
- net ESP32_GPIO19_CIPO: track 143.9 -> 0.00 mm, vias 5 -> 0
- net ESP32_GPIO19_CIPO8: track 143.9 -> 0.00 mm, vias 5 -> 0
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- added copper zone on layer 1, net GND12
- added copper zone on layer 16, net GND12
- added copper zone on layer 2, net GND12
- added copper zone on layer 1, net GND14
- added copper zone on layer 16, net GND14
- added copper zone on layer 2, net GND14
- added copper zone on layer 1, net GND16
- added copper zone on layer 16, net GND16
- added copper zone on layer 2, net GND16
- added copper zone on layer 1, net GND18
- added copper zone on layer 16, net GND18
- added copper zone on layer 2, net GND18
- added copper zone on layer 1, net GND20
- added copper zone on layer 16, net GND20
- added copper zone on layer 2, net GND20
- added copper zone on layer 1, net GND22
- added copper zone on layer 16, net GND22
- added copper zone on layer 2, net GND22
- removed copper zone on layer 1, net GND1
- removed copper zone on layer 16, net GND1
- removed copper zone on layer 2, net GND1
- removed copper zone on layer 1, net GND11
- removed copper zone on layer 16, net GND11
- removed copper zone on layer 2, net GND11
- removed copper zone on layer 1, net GND3
- removed copper zone on layer 16, net GND3
- removed copper zone on layer 2, net GND3
- removed copper zone on layer 1, net GND5
- removed copper zone on layer 16, net GND5
- removed copper zone on layer 2, net GND5
- removed copper zone on layer 1, net GND7
- removed copper zone on layer 16, net GND7
- removed copper zone on layer 2, net GND7
- removed copper zone on layer 1, net GND9
- removed copper zone on layer 16, net GND9
- removed copper zone on layer 2, net GND9
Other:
- board size 242.1 x 248.9 mm -> 254.3 x 248.9 mm

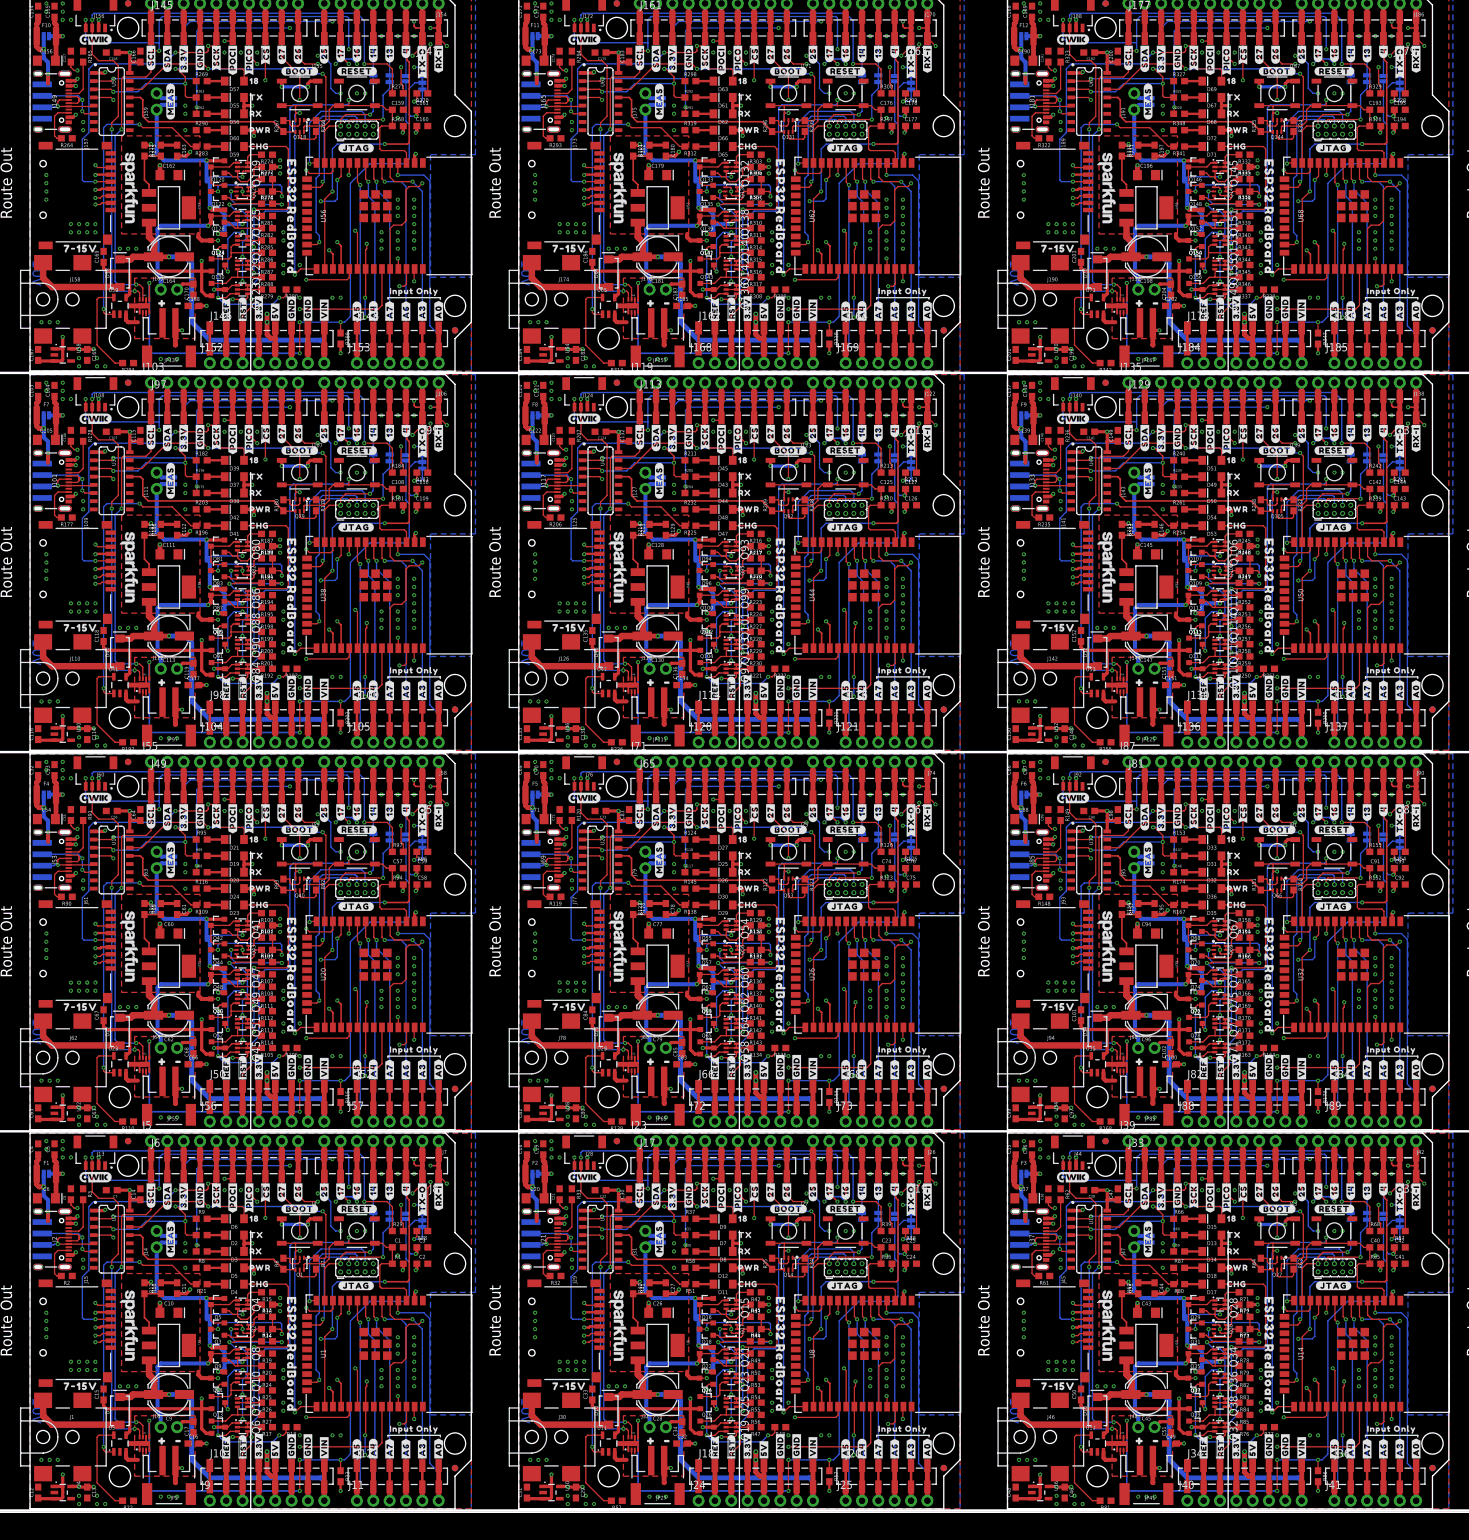
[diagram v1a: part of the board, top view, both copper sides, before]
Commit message: Moved SD card connector; updated RST/RESET flags.
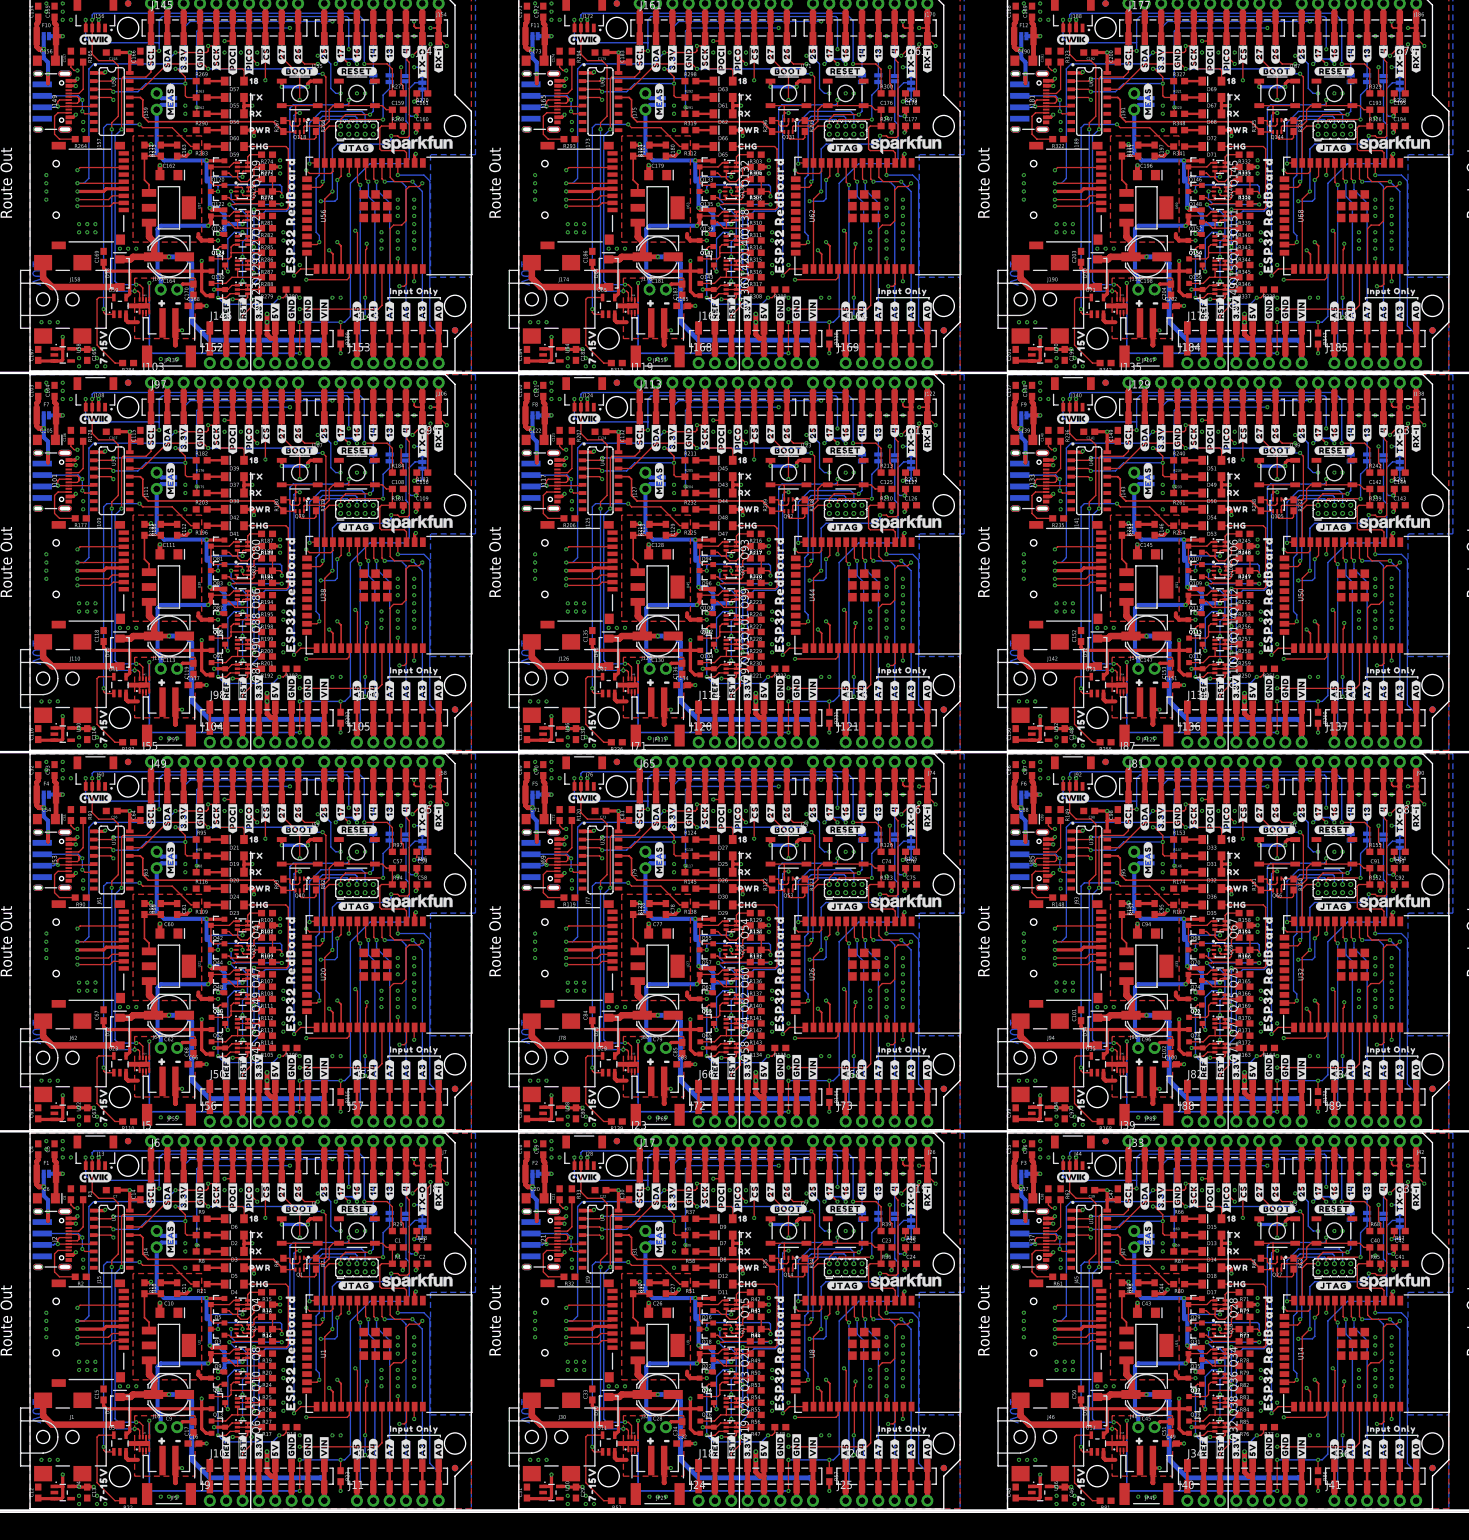
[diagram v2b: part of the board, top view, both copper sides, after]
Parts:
- moved LOGO11 45.3 mm to (212.1, 35.2), turned to 0 degrees
- moved LOGO26 45.3 mm to (212.1, 94.1), turned to 0 degrees
- moved LOGO41 45.3 mm to (212.1, 153.0), turned to 0 degrees
- moved LOGO56 45.3 mm to (212.1, 212.0), turned to 0 degrees
- moved LOGO1 45.3 mm to (60.2, 35.2), turned to 0 degrees
- moved LOGO16 45.3 mm to (60.2, 94.1), turned to 0 degrees
- moved LOGO21 45.3 mm to (136.1, 94.1), turned to 0 degrees
- moved LOGO31 45.3 mm to (60.2, 153.0), turned to 0 degrees
- moved LOGO36 45.3 mm to (136.1, 153.0), turned to 0 degrees
- moved LOGO46 45.3 mm to (60.2, 212.0), turned to 0 degrees
- moved LOGO5 45.3 mm to (136.1, 35.2), turned to 0 degrees
- moved LOGO51 45.3 mm to (136.1, 212.0), turned to 0 degrees
- moved U$140 19.8 mm to (116.5, 14.2), turned to 90 degrees
- moved U$234 19.8 mm to (192.4, 14.2), turned to 90 degrees
- moved U$48 19.8 mm to (40.5, 14.2), turned to 90 degrees
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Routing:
- net ESP32_GPIO23_PICO3: track 114.5 -> 122.7 mm
- net ESP32_GPIO23_PICO9: track 114.5 -> 122.7 mm
- net ESP32_GPIO23_PICO7: track 114.5 -> 122.7 mm
- net ESP32_GPIO23_PICO4: track 114.5 -> 122.7 mm
- net ESP32_GPIO23_PICO10: track 114.5 -> 122.7 mm
- net ESP32_GPIO23_PICO1: track 114.5 -> 122.7 mm
- net ESP32_GPIO23_PICO: track 114.5 -> 122.7 mm
- net ESP32_GPIO23_PICO6: track 114.5 -> 122.7 mm
- net ESP32_GPIO23_PICO5: track 114.5 -> 122.7 mm
- net ESP32_GPIO23_PICO2: track 114.5 -> 122.7 mm
- net ESP32_GPIO23_PICO8: track 114.5 -> 122.7 mm
- net ESP32_GPIO23_PICO11: track 114.5 -> 122.7 mm
- net ESP32_GPIO5_!CS!9: track 104.7 -> 112.4 mm
- net ESP32_GPIO5_!CS!7: track 104.7 -> 112.4 mm
- net ESP32_GPIO5_!CS!6: track 104.7 -> 112.4 mm
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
